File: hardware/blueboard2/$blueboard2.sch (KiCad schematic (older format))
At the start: 126 parts, among them Q1 TRANSISTOR_NPN, Q2 TRANSISTOR_NPN, Q3 TRANSISTOR_NPN, SW1 SW_SPST, SW2 SW_PUSHBUTTON

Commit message: round 2 of board design
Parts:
- removed BT1: BATTERY, Freetronics:1X02, symbol BATTERY
- removed SW1: SW_SPST, Freetronics:1X02, symbol SW_SPST
- added C1: 10uF, Freetronics:CAP_ELECTRO_D4S1.8, symbol CAP
- added JPG1, JPG2, JPG3, JPG4, JPVIN1: M01, Freetronics:1X01, symbol M01
- added MOUNT1, MOUNT2, MOUNT3, MOUNT4, MOUNT5: M01, Wire_Pads:SolderWirePad_single_2mmDrill, symbol M01
- HC1: footprint MODULE -> finn_kicad:HC05
- JP2: footprint Freetronics:1X07 -> Freetronics:1X01
- LDR1: renamed from R66; value RES_PHOTO_LDR -> LDR
- LDR10: renamed from R84; value RES_PHOTO_LDR -> LDR
- LDR11: renamed from R86; value RES_PHOTO_LDR -> LDR
- LDR12: renamed from R88; value RES_PHOTO_LDR -> LDR
- LDR13: renamed from R90; value RES_PHOTO_LDR -> LDR
- LDR14: renamed from R92; value RES_PHOTO_LDR -> LDR
- LDR15: renamed from R94; value RES_PHOTO_LDR -> LDR
- LDR16: renamed from R96; value RES_PHOTO_LDR -> LDR
- LDR2: renamed from R68; value RES_PHOTO_LDR -> LDR
- LDR3: renamed from R70; value RES_PHOTO_LDR -> LDR
- LDR4: renamed from R72; value RES_PHOTO_LDR -> LDR
- LDR5: renamed from R74; value RES_PHOTO_LDR -> LDR
- LDR6: renamed from R76; value RES_PHOTO_LDR -> LDR
- LDR7: renamed from R78; value RES_PHOTO_LDR -> LDR
- LDR8: renamed from R80; value RES_PHOTO_LDR -> LDR
- LDR9: renamed from R82; value RES_PHOTO_LDR -> LDR
- R98: footprint Resistors_ThroughHole:Resistor_Horizontal_RM15mm -> Resistors_ThroughHole:Resistor_Horizontal_RM10mm
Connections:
- net labels removed: VCC
- wire segments 385 -> 368
- no-connect marks 9 -> 20

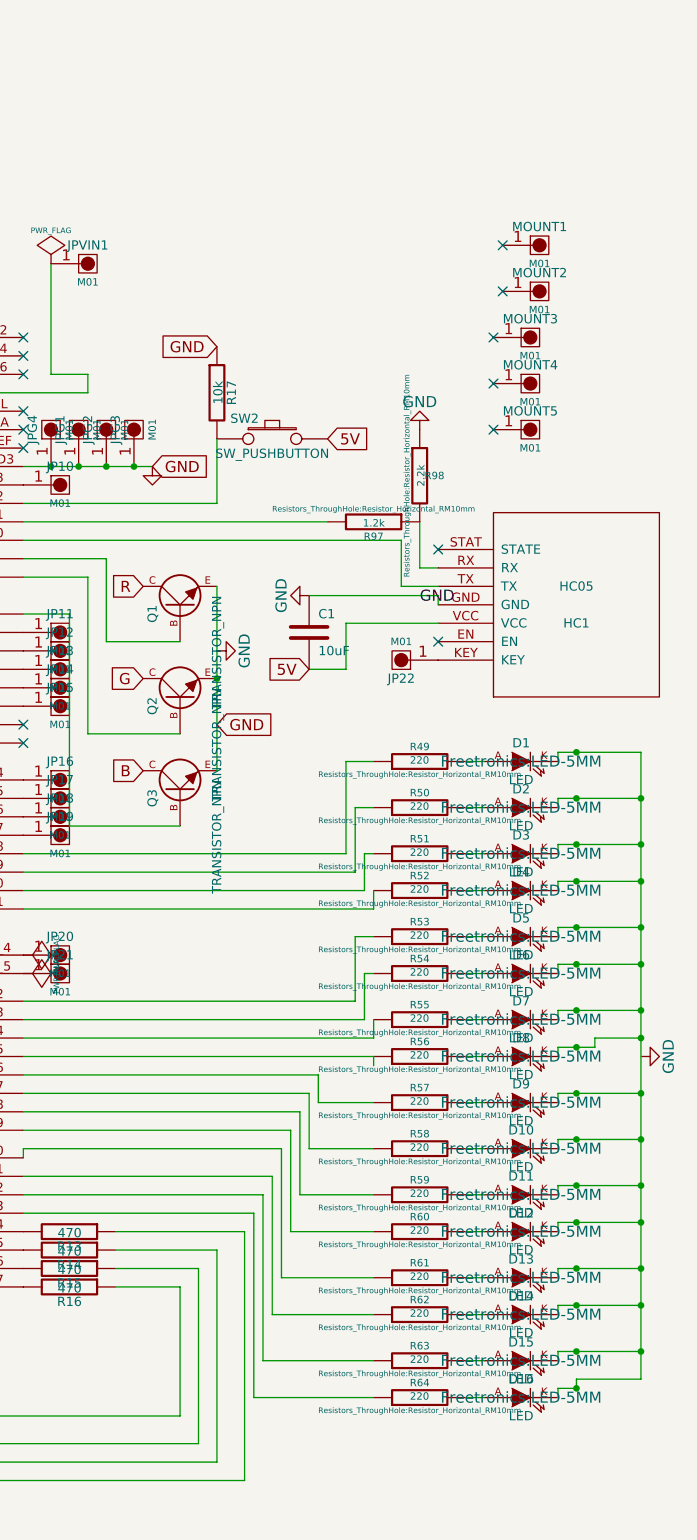
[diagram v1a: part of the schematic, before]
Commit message: state when board sent to manufacture
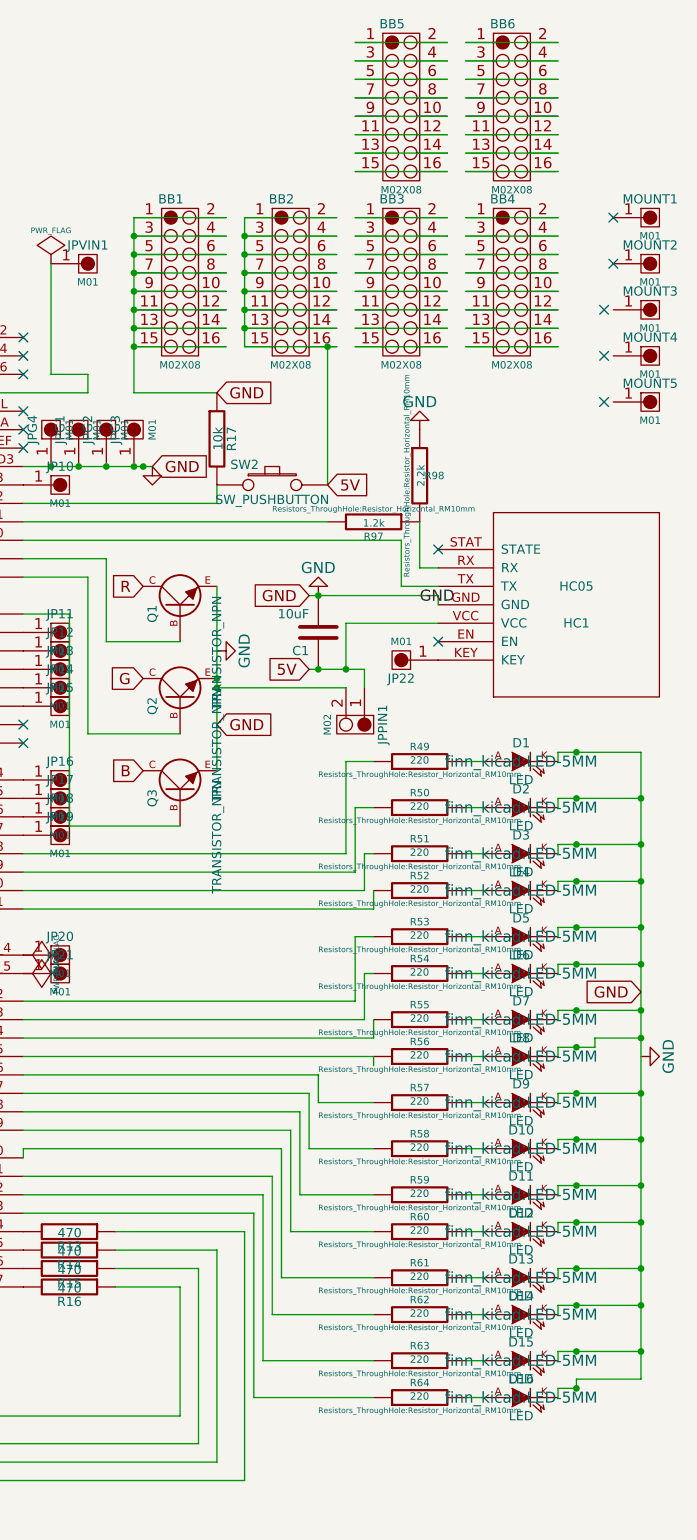
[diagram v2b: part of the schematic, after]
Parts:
- added BB1, BB2, BB3, BB4, BB5, BB6: M02X08, Freetronics:2X8, symbol M02X08
- added JPPIN1: M02, Freetronics:1X02, symbol M02
- D1, D10, D11, D12, D13, D14, D15, D16, D2, D3, D4, D5, D6, D7, D8, D9: footprint Freetronics:LED-5MM -> finn_kicad:LED-5MM
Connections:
- net 5V: now also C1.1, BB2.1, BB2.10, BB2.11, BB2.12, BB2.13, BB2.14, BB2.15, BB2.16, BB2.2, BB2.3, BB2.4, BB2.5, BB2.6, BB2.7, BB2.8, BB2.9, JPPIN1.1; no longer C1.2
- net GND: now also C1.2, D1.K, D10.K, D11.K, D12.K, D13.K, D14.K, D15.K, D16.K, D2.K, D3.K, D4.K, D5.K, D6.K, D7.K, D8.K, D9.K, BB1.1, BB1.10, BB1.11, BB1.12, BB1.13, BB1.14, BB1.15, BB1.16, BB1.2, BB1.3, BB1.4, BB1.5, BB1.6, BB1.7, BB1.8, BB1.9, JPPIN1.2; no longer C1.1
- new net: BB3.1, BB3.2
- new net: BB3.10, BB3.9
- new net: BB3.11, BB3.12
- new net: BB3.13, BB3.14
- new net: BB3.15, BB3.16
- new net: BB3.3, BB3.4
- new net: BB3.5, BB3.6
- new net: BB3.7, BB3.8
- new net: BB4.1, BB4.2
- new net: BB4.10, BB4.9
- new net: BB4.11, BB4.12
- new net: BB4.13, BB4.14
- new net: BB4.15, BB4.16
- new net: BB4.3, BB4.4
- new net: BB4.5, BB4.6
- new net: BB4.7, BB4.8
- new net: BB5.1, BB5.2
- new net: BB5.10, BB5.9
- new net: BB5.11, BB5.12
- new net: BB5.13, BB5.14
- new net: BB5.15, BB5.16
- new net: BB5.3, BB5.4
- new net: BB5.5, BB5.6
- new net: BB5.7, BB5.8
- new net: BB6.1, BB6.2
- new net: BB6.10, BB6.9
- new net: BB6.11, BB6.12
- new net: BB6.13, BB6.14
- new net: BB6.15, BB6.16
- new net: BB6.3, BB6.4
- new net: BB6.5, BB6.6
- new net: BB6.7, BB6.8
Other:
- moved on the sheet: C1, MOUNT1, MOUNT2, MOUNT3, MOUNT4, MOUNT5, R17, SW2
